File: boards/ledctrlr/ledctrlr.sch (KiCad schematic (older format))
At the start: 54 parts, among them IC1 ATMEGA168-P, IC2 SN75176B, J1 RJ45, J2 RJ45, SW1 SW_PUSH, U1 LM7805, X1 CRYSTAL

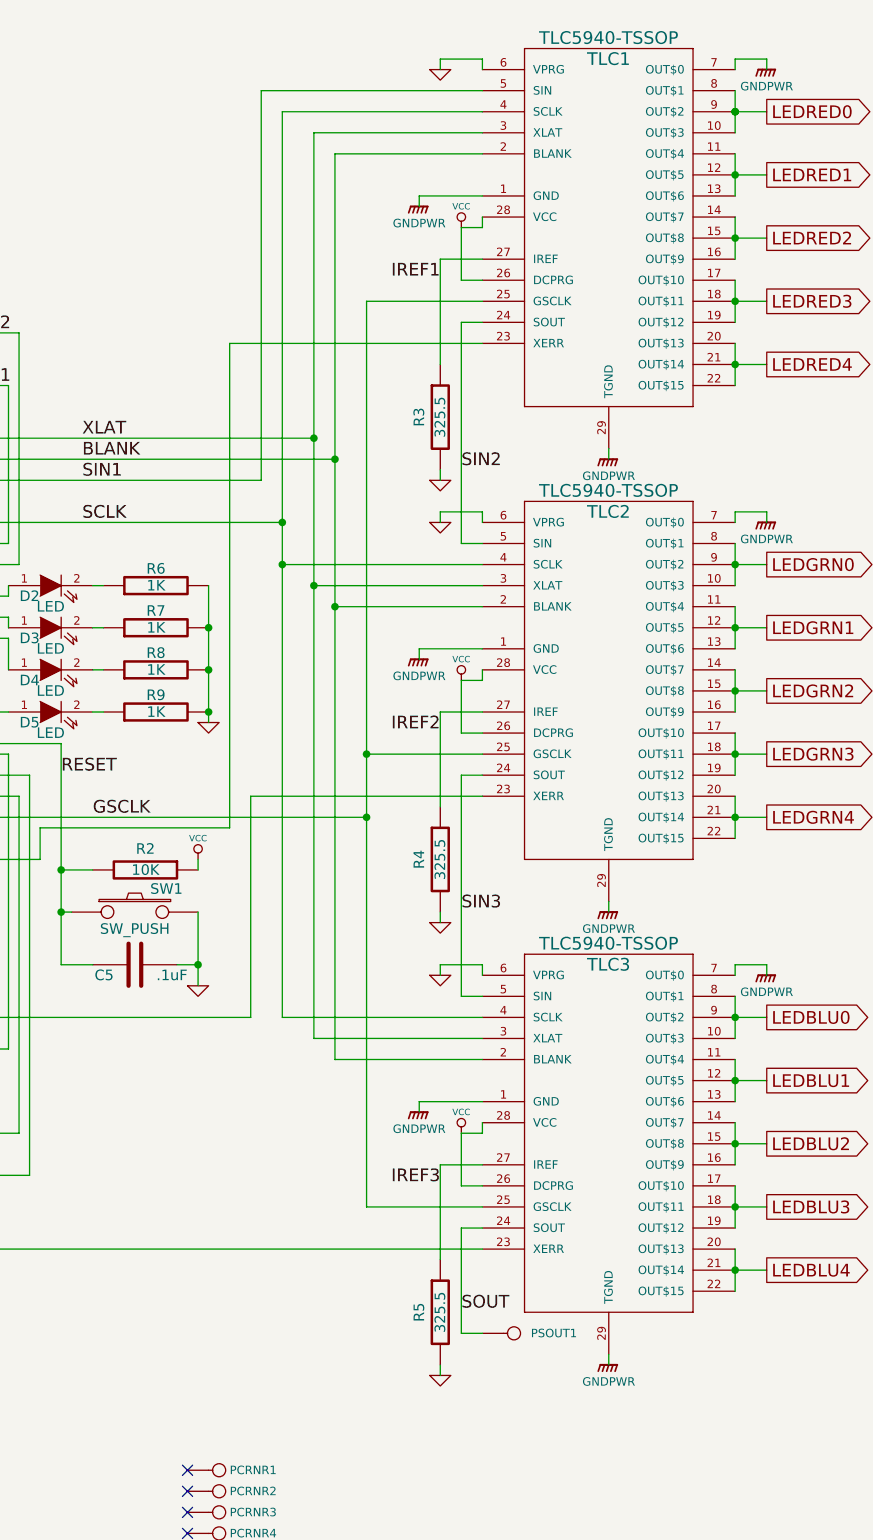
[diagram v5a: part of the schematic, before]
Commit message: begin ripup and design of new boards
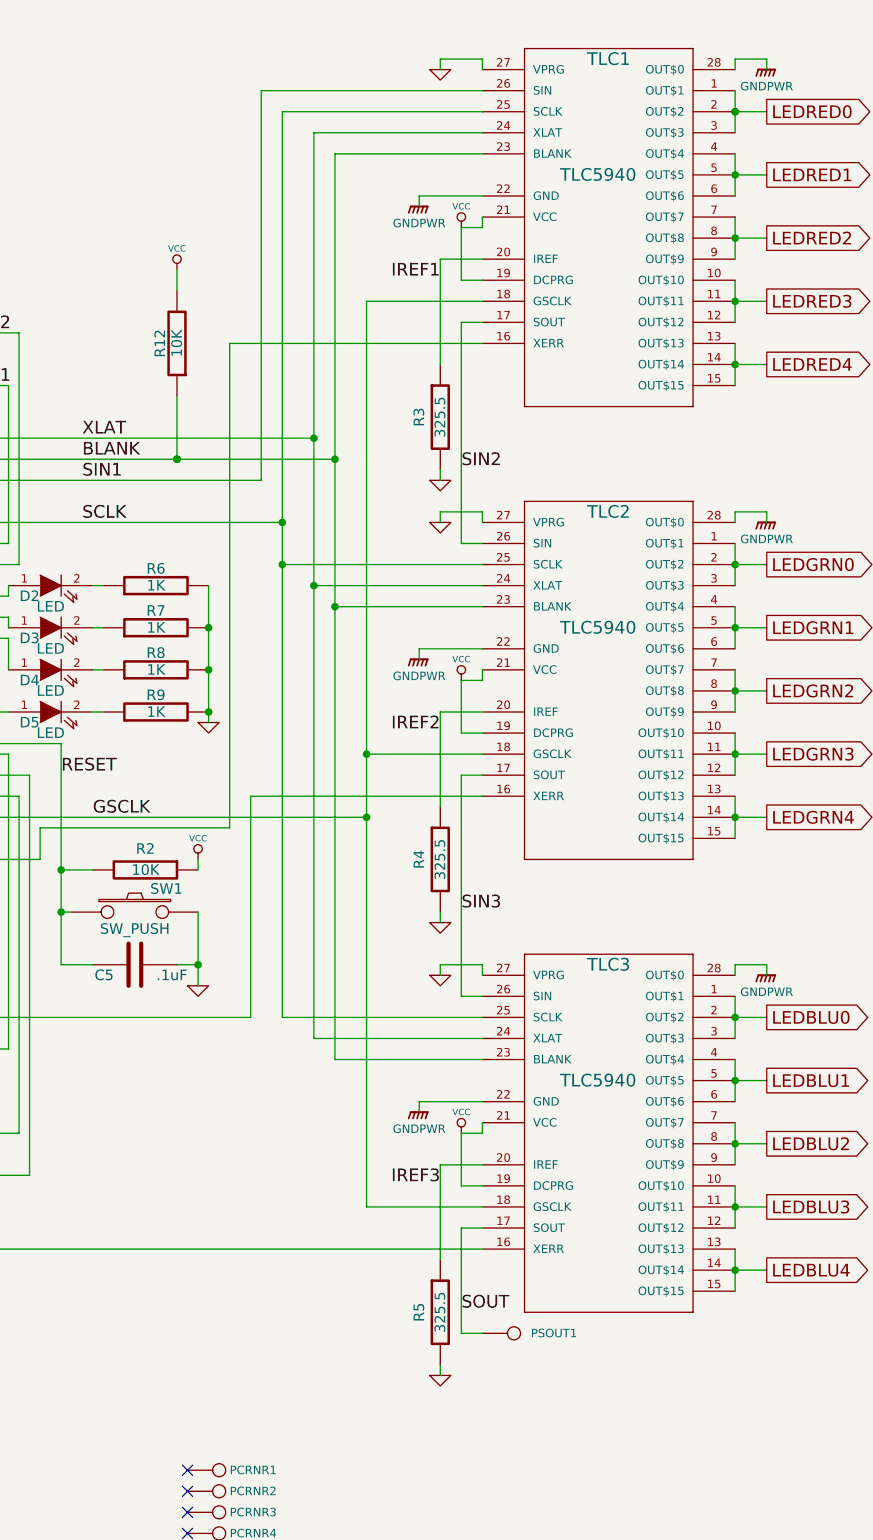
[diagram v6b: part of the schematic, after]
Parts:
- removed TLC1, TLC2, TLC3: TLC5940-TSSOP, tssop-28-thermal, symbol TLC5940-TSSOP
- added R12: 10K, SM0805, symbol R
- added TLC1, TLC2, TLC3: TLC5940, symbol TLC5940
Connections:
- net BLANK: now also R12.1, TLC1.23 (BLANK), TLC2.23 (BLANK), TLC3.23 (BLANK)
- net GND: now also TLC1.22 (GND), TLC1.27 (VPRG), TLC1.28 (OUT$0), TLC2.22 (GND), TLC2.27 (VPRG), TLC2.28 (OUT$0), TLC3.22 (GND), TLC3.27 (VPRG), TLC3.28 (OUT$0)
- net GSCLK: now also TLC1.18 (GSCLK), TLC2.18 (GSCLK), TLC3.18 (GSCLK)
- net IREF1: now also TLC1.20 (IREF)
- net IREF2: now also TLC2.20 (IREF)
- net IREF3: now also TLC3.20 (IREF)
- net LEDBLU0: now also TLC3.1 (OUT$1), TLC3.2 (OUT$2), TLC3.3 (OUT$3)
- net LEDBLU1: now also TLC3.4 (OUT$4), TLC3.5 (OUT$5), TLC3.6 (OUT$6)
- net LEDBLU2: now also TLC3.7 (OUT$7), TLC3.8 (OUT$8), TLC3.9 (OUT$9)
- net LEDBLU3: now also TLC3.10 (OUT$10), TLC3.11 (OUT$11), TLC3.12 (OUT$12)
- net LEDBLU4: now also TLC3.13 (OUT$13), TLC3.14 (OUT$14), TLC3.15 (OUT$15)
- net LEDGRN0: now also TLC2.1 (OUT$1), TLC2.2 (OUT$2), TLC2.3 (OUT$3)
- net LEDGRN1: now also TLC2.4 (OUT$4), TLC2.5 (OUT$5), TLC2.6 (OUT$6)
- net LEDGRN2: now also TLC2.7 (OUT$7), TLC2.8 (OUT$8), TLC2.9 (OUT$9)
- net LEDGRN3: now also TLC2.10 (OUT$10), TLC2.11 (OUT$11), TLC2.12 (OUT$12)
- net LEDGRN4: now also TLC2.13 (OUT$13), TLC2.14 (OUT$14), TLC2.15 (OUT$15)
- net LEDRED0: now also TLC1.1 (OUT$1), TLC1.2 (OUT$2), TLC1.3 (OUT$3)
- net LEDRED1: now also TLC1.4 (OUT$4), TLC1.5 (OUT$5), TLC1.6 (OUT$6)
- net LEDRED2: now also TLC1.7 (OUT$7), TLC1.8 (OUT$8), TLC1.9 (OUT$9)
- net LEDRED3: now also TLC1.10 (OUT$10), TLC1.11 (OUT$11), TLC1.12 (OUT$12)
- net LEDRED4: now also TLC1.13 (OUT$13), TLC1.14 (OUT$14), TLC1.15 (OUT$15)
- net SCLK: now also TLC1.25 (SCLK), TLC2.25 (SCLK), TLC3.25 (SCLK)
- net SIN1: now also TLC1.26 (SIN)
- net SIN2: now also TLC1.17 (SOUT), TLC2.26 (SIN)
- net SIN3: now also TLC2.17 (SOUT), TLC3.26 (SIN)
- net SOUT: now also TLC3.17 (SOUT)
- net VCC: now also R12.2, TLC1.19 (DCPRG), TLC1.21 (VCC), TLC2.19 (DCPRG), TLC2.21 (VCC), TLC3.19 (DCPRG), TLC3.21 (VCC)
- net XERR1: now also TLC1.16 (XERR)
- net XERR2: now also TLC2.16 (XERR)
- net XERR3: now also TLC3.16 (XERR)
- net XLAT: now also TLC1.24 (XLAT), TLC2.24 (XLAT), TLC3.24 (XLAT)
